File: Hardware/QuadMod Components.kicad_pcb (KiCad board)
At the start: 4 copper layers, 70.6 x 100 mm, 122 parts, among them J1 Conn_01x08_Pin, J2 Conn_01x08_Pin, J3 Conn_01x08_Pin, J4 Conn_01x08_Pin, J5 Eurorack_10_pin_power, J6 USB_B_Micro, J7 Prog_Header, J8 Extra_Outs, J9 Test_Outs, U1 LD1117-3.3-4Tab, U2 STM32H563VIT, U3 TL072, U4 MCP6004, U5 TPS561201, U6 MCP6004, U7 MCP6002-xSN, U8 STF202-22T1G, U9 AK4619VN, Y1 8MHz 20pF

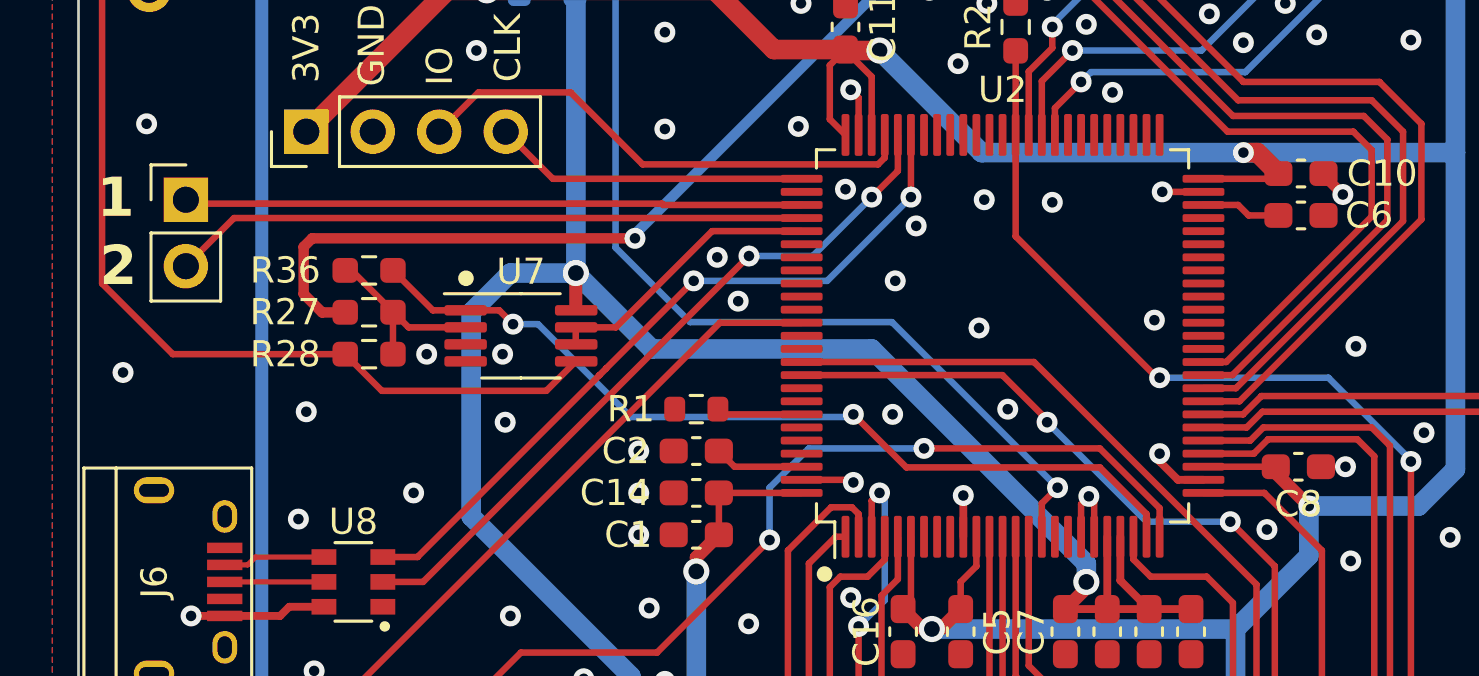
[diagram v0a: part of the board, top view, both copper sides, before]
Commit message: Updated Production Gerbers; attempts to get USB working with O1 optimisation
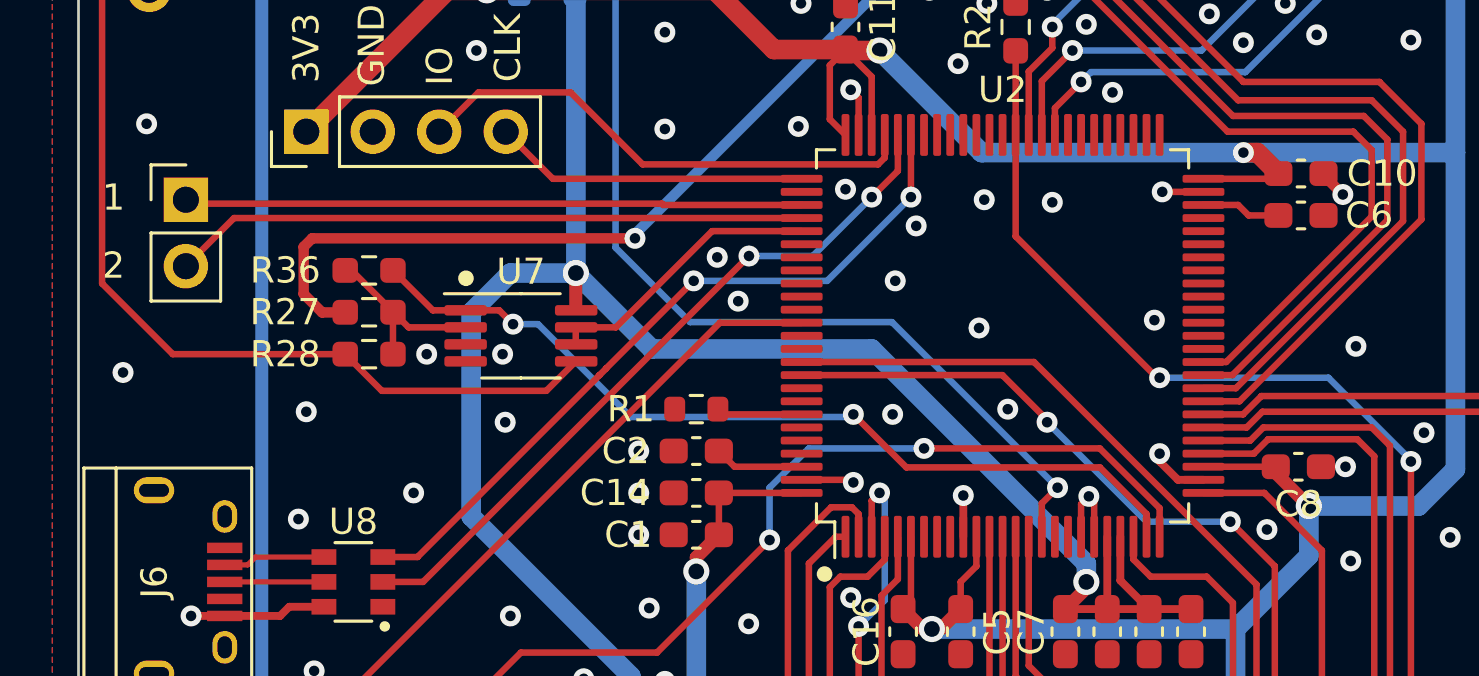
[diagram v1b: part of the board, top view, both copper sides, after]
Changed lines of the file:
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@@
     (effects (font (size 1 1) (thickness 0.15)))
   )
-  (gr_text "1" (at 100.7 95.6) (layer "F.SilkS")
-    (effects (font (size 1.5 1.5) (thickness 0.3) bold) (justify left bottom))
-  )
-  (gr_text "2" (at 100.8 98.2) (layer "F.SilkS")
-    (effects (font (size 1.5 1.5) (thickness 0.3) bold) (justify left bottom))
+  (gr_text "1" (at 100.9 95.3) (layer "F.SilkS")
+    (effects (font (size 1 1) (thickness 0.1875)) (justify left bottom))
+  )
+  (gr_text "2" (at 100.9 97.9) (layer "F.SilkS")
+    (effects (font (size 1 1) (thickness 0.1875)) (justify left bottom))
   )
   (gr_text "DAC3" (at 163.6 118.6) (layer "F.SilkS")
@@
   (via (at 149.45 69.85) (size 1) (drill 0.6) (layers "F.Cu" "B.Cu") (net 2))
   (via (at 115.6 86.8) (size 1) (drill 0.6) (layers "F.Cu" "B.Cu") (net 2))
-  (via (at 147 106.5) (size 0.8) (drill 0.4) (layers "F.Cu" "B.Cu") (net 2))
+  (via (at 147 106.5) (size 1) (drill 0.6) (layers "F.Cu" "B.Cu") (net 2))
   (via (at 132.6 111.2) (size 1) (drill 0.6) (layers "F.Cu" "B.Cu") (net 2))
   (segment (start 134.5 93) (end 144.5 93) (width 0.75) (layer "B.Cu") (net 2))
